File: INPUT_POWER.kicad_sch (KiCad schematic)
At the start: 26 parts, among them J1 TYPE-C-31-M12_13, SW3 ON/OFF, U3 IP5306

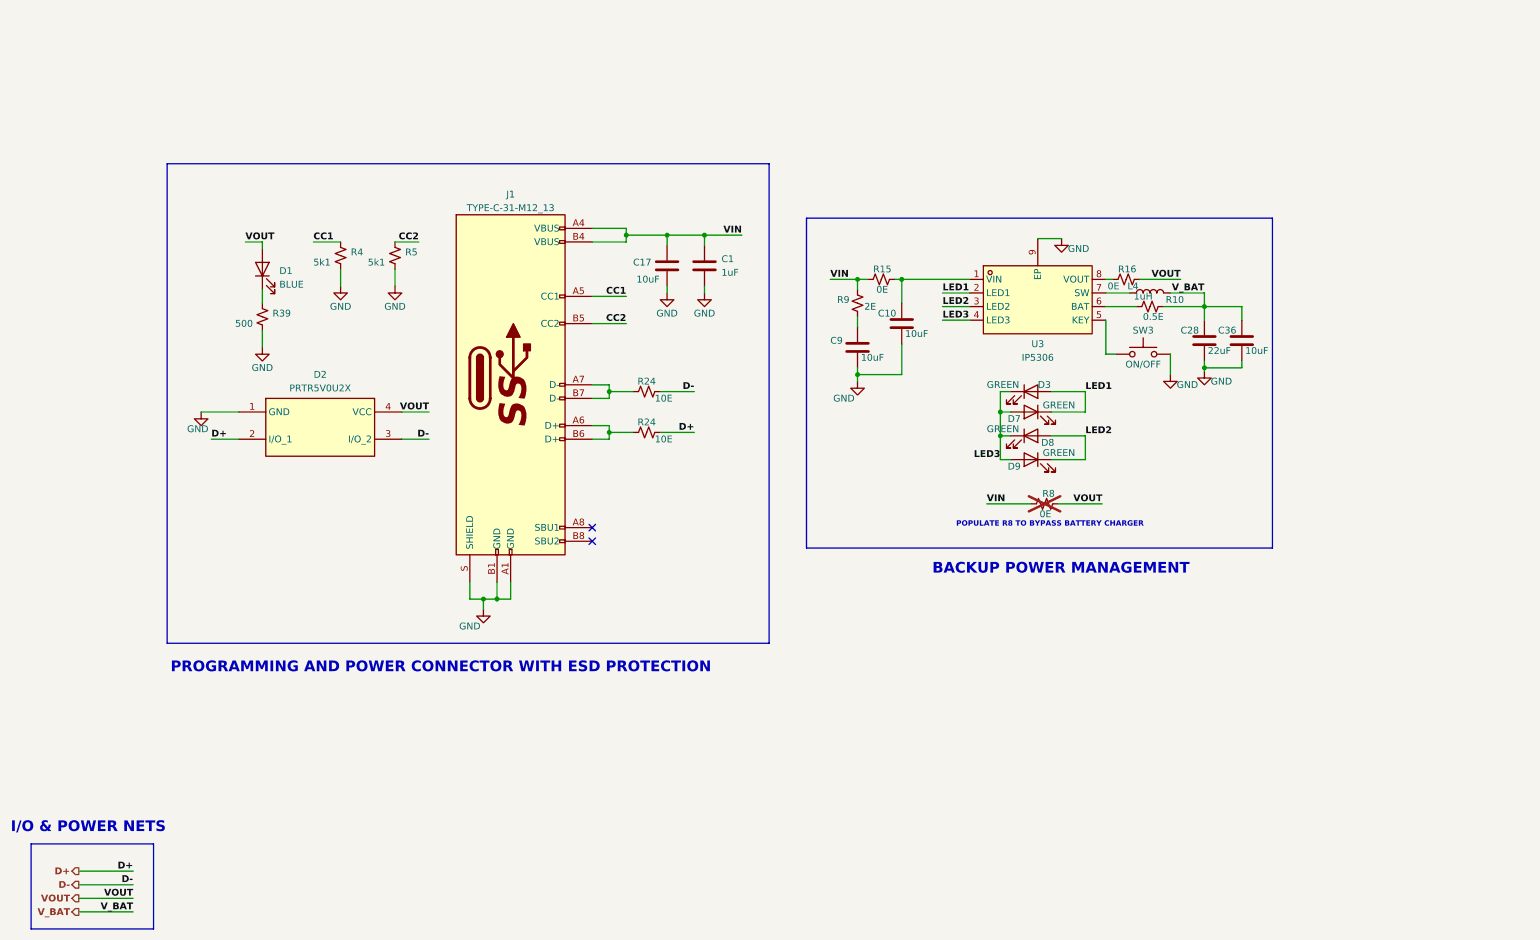
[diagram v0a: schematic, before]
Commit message: Corrected schematic to PCB export error and warings and IP5306 and SD card section
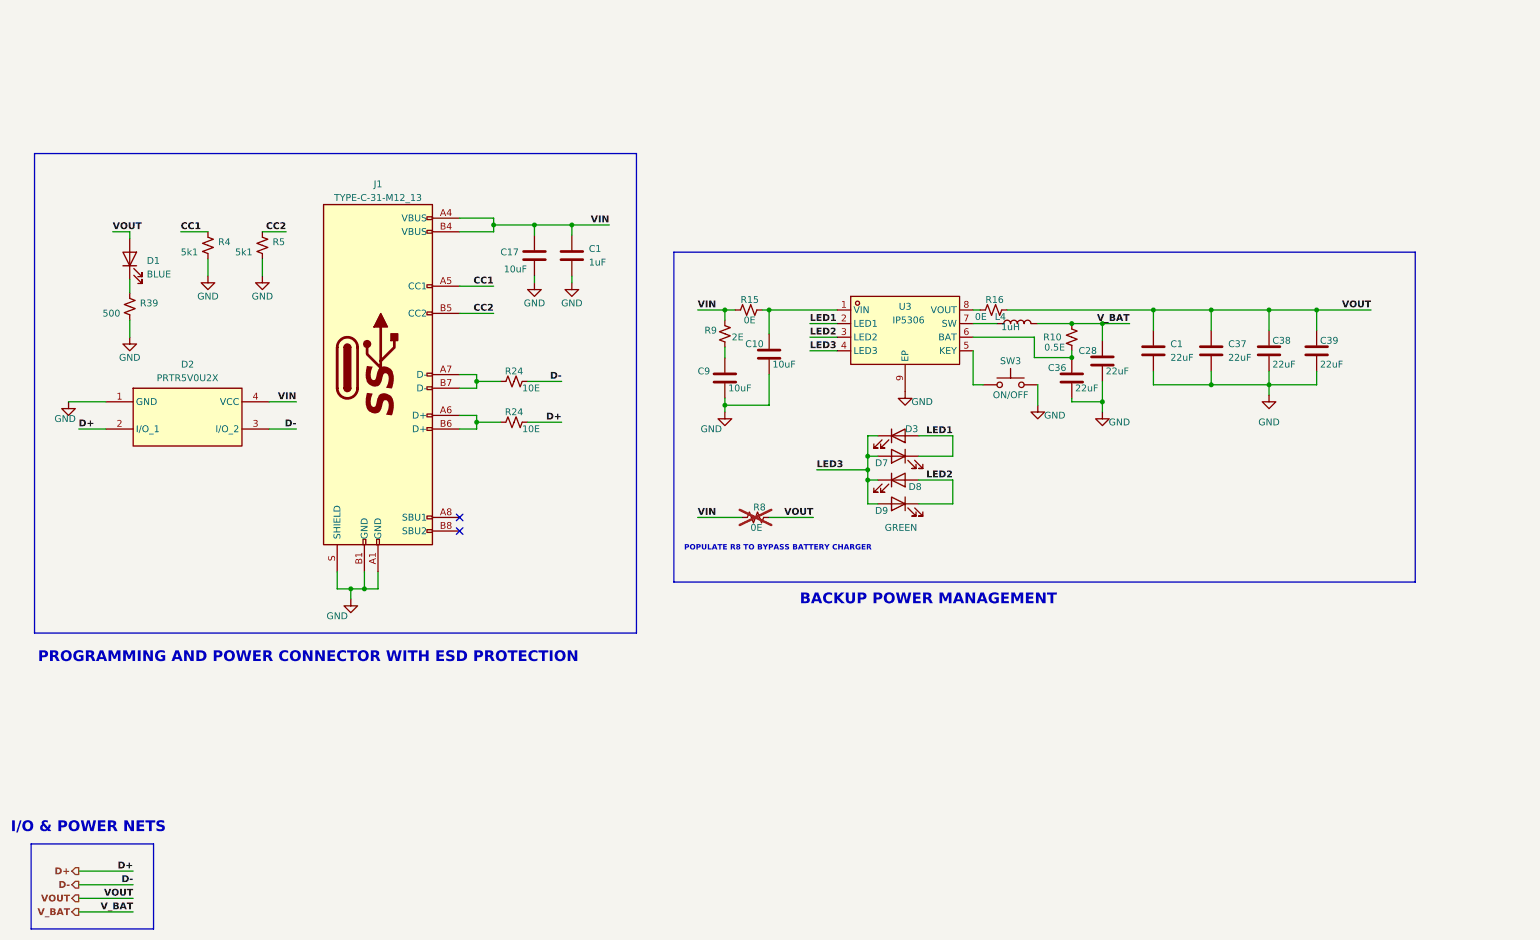
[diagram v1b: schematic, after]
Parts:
- added C1, C37, C38, C39: 22uF, ESP32-S3_Dev_Board:C_1206_3216Metric, symbol ESP32-S3_DB:C
- C36: value 10uF -> 22uF; footprint ESP32-S3_Dev_Board:C_0805_2012Metric -> ESP32-S3_Dev_Board:C_0603_1608Metric; PN CL21A106KAYNNNE -> CL10A226MO7JZNC
- U3: footprint ESP32-S3_Dev_Board:ESOP-8_L4.9-W3.9-P1.27-LS6.0-BL-EP -> ESP32-S3_Dev_Board:ESOP-8
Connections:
- net GND: now also C1.2, C37.2, C38.2, C39.2
- net VIN: now also D2.4 (VCC)
- net VOUT: now also C1.1, C37.1, C38.1, C39.1; no longer D2.4 (VCC)
- net V_BAT: no longer C36.1
- net at R10.1, U3.6 (BAT): now also C36.1
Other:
- moved on the sheet: C1, C10, C17, C28, C9, D1, D2, D3, D7, D8, D9, J1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

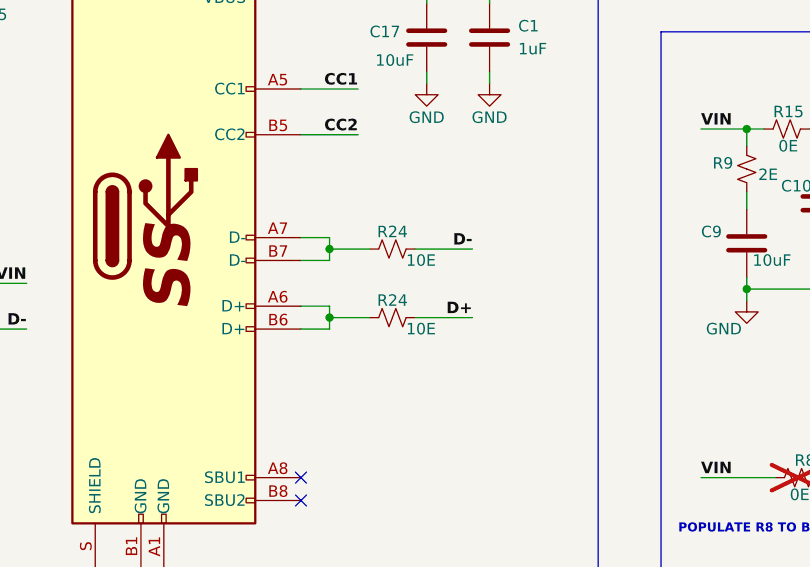
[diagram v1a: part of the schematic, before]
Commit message: Changes CH340 schematic
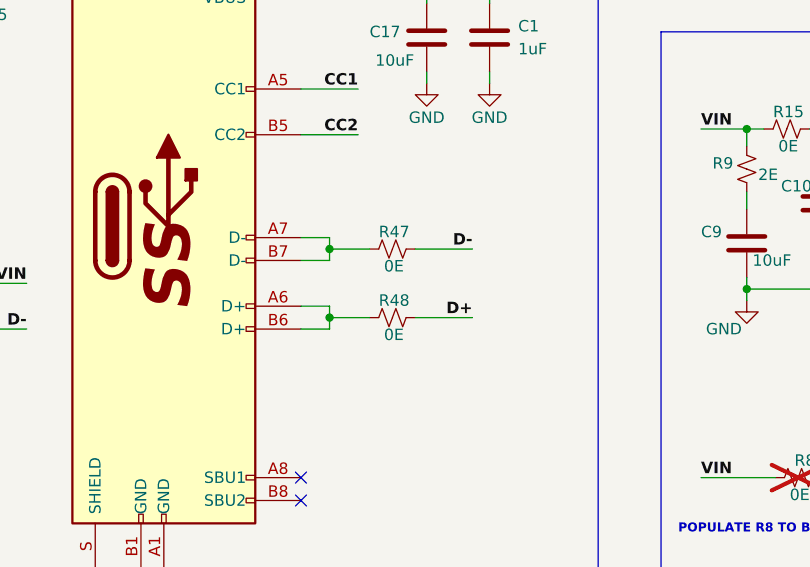
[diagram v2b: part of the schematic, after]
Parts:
- removed R24 (x2): 10E, ESP32-S3_Dev_Board:R_0402_1005Metric, symbol ESP32-S3_DB:R_Small_US
- added R47, R48: 0E, ESP32-S3_Dev_Board:R_0603_1608Metric, symbol ESP32-S3_DB:R_Small_US
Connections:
- net D+: now also R48.2
- net D-: now also R47.2
- net at J1.A7 (D-), J1.B7 (D-): now also R47.1
- net at J1.A6 (D+), J1.B6 (D+): now also R48.1
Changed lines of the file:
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@@
-    )
-  )
-  (symbol (lib_id "ESP32-S3_DB:R_Small_US") (at 109.855 86.36 90) (unit 1)
-    (in_bom yes) (on_board yes) (dnp no)
-    (property "Reference" "R24" (at 109.855 84.455 90)
-      (effects (font (size 1.27 1.27)))
-    )
-    (property "Value" "10E" (at 113.03 87.63 90)
-      (effects (font (size 1.27 1.27)))
-    )
-    (property "Footprint" "ESP32-S3_Dev_Board:R_0402_1005Metric" (at 109.855 86.36 0)
-      (effects (font (size 1.27 1.27)) hide)
-    )
-    (property "Datasheet" "~" (at 109.855 86.36 0)
-      (effects (font (size 1.27 1.27)) hide)
-    )
-    (property "PN" "RTT02100JTH" (at 109.855 86.36 0)
-      (effects (font (size 1.27 1.27)) hide)
-    )
-    (pin "1")
-    (pin "2")
-    (instances
-      (project "ESP32-S3_DB"
-        (path "/b7fc4bd3-c219-4455-832b-8d795385dcf1/9b4afe2f-79e5-4a56-98d7-d16b193c0e70"
-          (reference "R24") (unit 1)
-        )
-        (path "/b7fc4bd3-c219-4455-832b-8d795385dcf1/95090a63-7b3c-4ea0-92b8-aeafe05264cd"
-          (reference "R47") (unit 1)
-        )
-      )
-    )
-  )
-  (symbol (lib_id "ESP32-S3_DB:R_Small_US") (at 109.855 93.98 90) (unit 1)
-    (in_bom yes) (on_board yes) (dnp no)
-    (property "Reference" "R24" (at 109.855 92.075 90)
-      (effects (font (size 1.27 1.27)))
-    )
-    (property "Value" "10E" (at 113.03 95.25 90)
-      (effects (font (size 1.27 1.27)))
-    )
-    (property "Footprint" "ESP32-S3_Dev_Board:R_0402_1005Metric" (at 109.855 93.98 0)
-      (effects (font (size 1.27 1.27)) hide)
-    )
-    (property "Datasheet" "~" (at 109.855 93.98 0)
-      (effects (font (size 1.27 1.27)) hide)
-    )
-    (property "PN" "RTT02100JTH" (at 109.855 93.98 0)
-      (effects (font (size 1.27 1.27)) hide)
-    )
-    (pin "1")
-    (pin "2")
-    (instances
-      (project "ESP32-S3_DB"
-        (path "/b7fc4bd3-c219-4455-832b-8d795385dcf1/9b4afe2f-79e5-4a56-98d7-d16b193c0e70"
-          (reference "R24") (unit 1)
-        )
-        (path "/b7fc4bd3-c219-4455-832b-8d795385dcf1/95090a63-7b3c-4ea0-92b8-aeafe05264cd"
-          (reference "R48") (unit 1)
-        )
-      )
     )
   )
@@
         (path "/b7fc4bd3-c219-4455-832b-8d795385dcf1/95090a63-7b3c-4ea0-92b8-aeafe05264cd"
           (reference "R5") (unit 1)
+        )
+      )
+    )
+  )
+  (symbol (lib_id "ESP32-S3_DB:R_Small_US") (at 109.855 93.98 90) (unit 1)
+    (in_bom yes) (on_board yes) (dnp no)
+    (property "Reference" "R48" (at 111.76 92.075 90)
+      (effects (font (size 1.27 1.27)) (justify left))
+    )
+    (property "Value" "0E" (at 111.125 95.885 90)
+      (effects (font (size 1.27 1.27)) (justify left))
+    )
+    (property "Footprint" "ESP32-S3_Dev_Board:R_0603_1608Metric" (at 109.855 93.98 0)
+      (effects (font (size 1.27 1.27)) hide)
+    )
+    (property "Datasheet" "~" (at 109.855 93.98 0)
+      (effects (font (size 1.27 1.27)) hide)
+    )
+    (property "PN" "RC0603JR-070RL" (at 109.855 93.98 0)
+      (effects (font (size 1.27 1.27)) hide)
+    )
+    (pin "1")
+    (pin "2")
+    (instances
+      (project "ESP32-S3_DB"
+        (path "/b7fc4bd3-c219-4455-832b-8d795385dcf1/95090a63-7b3c-4ea0-92b8-aeafe05264cd"
+          (reference "R48") (unit 1)
         )
       )
@@
         )
       )
+    )
+  )
+  (symbol (lib_id "ESP32-S3_DB:R_Small_US") (at 109.855 86.36 90) (unit 1)
+    (in_bom yes) (on_board yes) (dnp no)
+    (property "Reference" "R47" (at 111.76 84.455 90)
+      (effects (font (size 1.27 1.27)) (justify left))
+    )
+    (property "Value" "0E" (at 111.125 88.265 90)
+      (effects (font (size 1.27 1.27)) (justify left))
+    )
+    (property "Footprint" "ESP32-S3_Dev_Board:R_0603_1608Metric" (at 109.855 86.36 0)
+      (effects (font (size 1.27 1.27)) hide)
+    )
+    (property "Datasheet" "~" (at 109.855 86.36 0)
+      (effects (font (size 1.27 1.27)) hide)
+    )
+    (property "PN" "RC0603JR-070RL" (at 109.855 86.36 0)
+      (effects (font (size 1.27 1.27)) hide)
+    )
+    (pin "1")
+    (pin "2")
+    (instances
+      (project "ESP32-S3_DB"
+        (path "/b7fc4bd3-c219-4455-832b-8d795385dcf1/95090a63-7b3c-4ea0-92b8-aeafe05264cd"
+          (reference "R47") (unit 1)
+        )
+      )

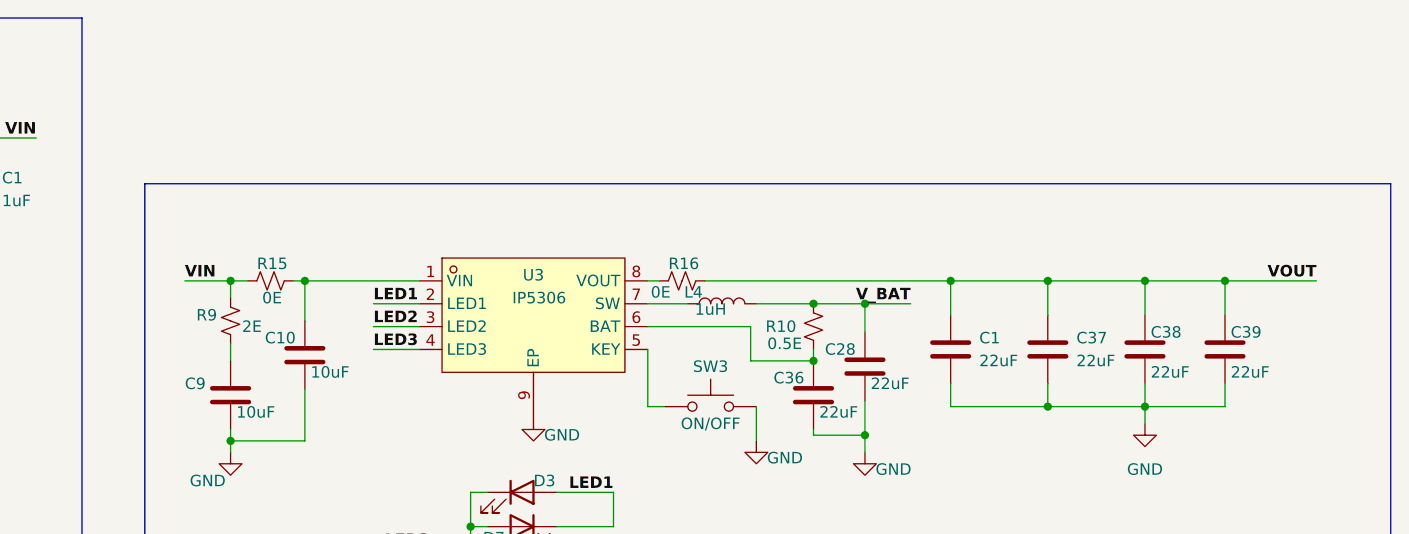
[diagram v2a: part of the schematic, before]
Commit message: Arranged IP5306, Added support for USB-To-RS485
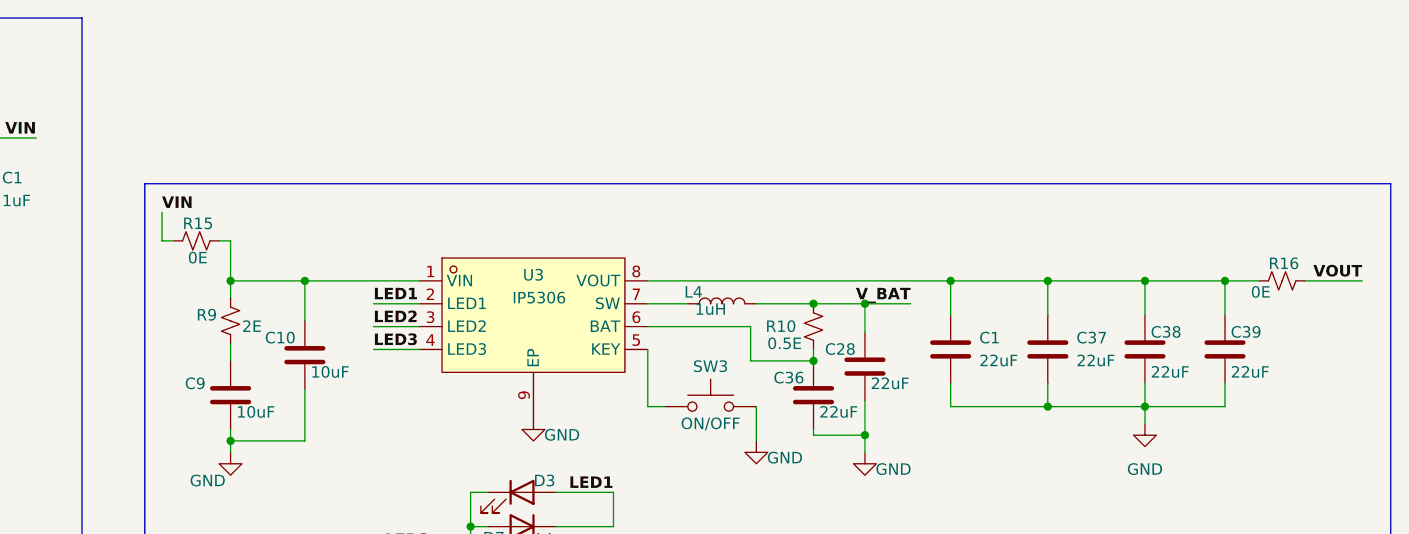
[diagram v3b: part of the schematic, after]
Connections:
- net VIN: no longer R9.1
- net VOUT: no longer C1.1, C37.1, C38.1, C39.1
- net at R16.1, U3.8 (VOUT): now also C1.1, C37.1, C38.1, C39.1
- net at C10.1, R15.2, U3.1 (VIN): now also R9.1
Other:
- moved on the sheet: R15, R16
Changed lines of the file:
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@@
     (stroke (width 1) (type default) (color 72 72 72 1))
   )
-  (wire (pts (xy 201.93 73.025) (xy 229.235 73.025))
+  (wire (pts (xy 195.58 73.025) (xy 229.235 73.025))
     (stroke (width 0) (type default))
   )
@@
     (stroke (width 0) (type default))
   )
+  (wire (pts (xy 141.605 65.405) (xy 141.605 68.58))
+    (stroke (width 0) (type default))
+  )
   (wire (pts (xy 149.225 74.93) (xy 149.225 73.025))
     (stroke (width 0) (type default))
@@
     (stroke (width 0.5) (type default) (color 0 0 255 1))
   )
-  (wire (pts (xy 196.85 73.025) (xy 195.58 73.025))
-    (stroke (width 0) (type default))
-  )
   (wire (pts (xy 165.1 75.565) (xy 170.18 75.565))
     (stroke (width 0) (type default))
@@
     (stroke (width 0.5) (type default) (color 255 0 0 1))
   )
+  (wire (pts (xy 141.605 68.58) (xy 142.875 68.58))
+    (stroke (width 0) (type default))
+  )
   (wire (pts (xy 207.645 90.805) (xy 207.645 86.995))
     (stroke (width 0) (type default))
@@
   )
   (wire (pts (xy 144.145 111.76) (xy 152.4 111.76))
+    (stroke (width 0) (type default))
+  )
+  (wire (pts (xy 147.955 68.58) (xy 149.225 68.58))
     (stroke (width 0) (type default))
   )
@@
     (stroke (width 0) (type default))
   )
-  (wire (pts (xy 156.21 73.025) (xy 157.48 73.025))
-    (stroke (width 0) (type default))
-  )
   (wire (pts (xy 67.31 58.42) (xy 62.865 58.42))
     (stroke (width 0) (type default))
   )
   (wire (pts (xy 102.87 86.36) (xy 102.87 87.63))
+    (stroke (width 0) (type default))
+  )
+  (wire (pts (xy 268.605 73.025) (xy 274.955 73.025))
     (stroke (width 0) (type default))
   )
@@
     (stroke (width 0) (type default))
   )
-  (wire (pts (xy 144.145 73.025) (xy 149.225 73.025))
-    (stroke (width 0) (type default))
-  )
   (wire (pts (xy 106.045 58.42) (xy 99.695 58.42))
     (stroke (width 0) (type default))
@@
     (stroke (width 0) (type default))
   )
-  (wire (pts (xy 259.715 73.025) (xy 269.875 73.025))
-    (stroke (width 0) (type default))
-  )
-  (wire (pts (xy 149.225 73.025) (xy 151.13 73.025))
+  (wire (pts (xy 259.715 73.025) (xy 263.525 73.025))
+    (stroke (width 0) (type default))
+  )
+  (wire (pts (xy 149.225 73.025) (xy 157.48 73.025))
+    (stroke (width 0) (type default))
+  )
+  (wire (pts (xy 149.225 68.58) (xy 149.225 73.025))
     (stroke (width 0) (type default))
   )
@@
     (effects (font (size 1.27 1.27) (thickness 0.254) bold (color 0 0 255 1)) (justify left bottom))
   )
-  (label "VOUT" (at 269.875 73.025 180) (fields_autoplaced)
+  (label "VOUT" (at 274.955 73.025 180) (fields_autoplaced)
     (effects (font (size 1.27 1.27) bold (color 255 0 0 1)) (justify right bottom))
   )
-  (label "VIN" (at 144.145 73.025 0) (fields_autoplaced)
+  (label "VIN" (at 141.605 65.405 0) (fields_autoplaced)
     (effects (font (size 1.27 1.27) (thickness 0.254) bold (color 255 0 0 1)) (justify left bottom))
   )
@@
     )
   )
-  (symbol (lib_id "ESP32-S3_DB:R_Small_US") (at 199.39 73.025 90) (unit 1)
-    (in_bom yes) (on_board yes) (dnp no)
-    (property "Reference" "R16" (at 201.295 71.12 90)
-      (effects (font (size 1.27 1.27)) (justify left))
-    )
-    (property "Value" "0E" (at 198.12 74.295 90)
-      (effects (font (size 1.27 1.27)) (justify left))
-    )
-    (property "Footprint" "ESP32-S3_Dev_Board:R_0603_1608Metric" (at 199.39 73.025 0)
-      (effects (font (size 1.27 1.27)) hide)
-    )
-    (property "Datasheet" "~" (at 199.39 73.025 0)
-      (effects (font (size 1.27 1.27)) hide)
-    )
-    (property "PN" "RC0603JR-070RL" (at 199.39 73.025 0)
+  (symbol (lib_id "ESP32-S3_DB:R_Small_US") (at 266.065 73.025 90) (unit 1)
+    (in_bom yes) (on_board yes) (dnp no)
+    (property "Reference" "R16" (at 267.97 71.12 90)
+      (effects (font (size 1.27 1.27)) (justify left))
+    )
+    (property "Value" "0E" (at 264.795 74.295 90)
+      (effects (font (size 1.27 1.27)) (justify left))
+    )
+    (property "Footprint" "ESP32-S3_Dev_Board:R_0603_1608Metric" (at 266.065 73.025 0)
+      (effects (font (size 1.27 1.27)) hide)
+    )
+    (property "Datasheet" "~" (at 266.065 73.025 0)
+      (effects (font (size 1.27 1.27)) hide)
+    )
+    (property "PN" "RC0603JR-070RL" (at 266.065 73.025 0)
       (effects (font (size 1.27 1.27)) hide)
     )
@@
     )
   )
-  (symbol (lib_id "ESP32-S3_DB:R_Small_US") (at 153.67 73.025 90) (unit 1)
-    (in_bom yes) (on_board yes) (dnp no)
-    (property "Reference" "R15" (at 155.575 71.12 90)
-      (effects (font (size 1.27 1.27)) (justify left))
-    )
-    (property "Value" "0E" (at 154.94 74.93 90)
-      (effects (font (size 1.27 1.27)) (justify left))
-    )
-    (property "Footprint" "ESP32-S3_Dev_Board:R_0603_1608Metric" (at 153.67 73.025 0)
-      (effects (font (size 1.27 1.27)) hide)
-    )
-    (property "Datasheet" "~" (at 153.67 73.025 0)
-      (effects (font (size 1.27 1.27)) hide)
-    )
-    (property "PN" "RC0603JR-070RL" (at 153.67 73.025 0)
-      (effects (font (size 1.27 1.27)) hide)
-    )
+  (symbol (lib_id "ESP32-S3_DB:R_Small_US") (at 145.415 68.58 90) (unit 1)
+    (in_bom yes) (on_board yes) (dnp no)
+    (property "Reference" "R15" (at 147.32 66.675 90)
+      (effects (font (size 1.27 1.27)) (justify left))
+    )
+    (property "Value" "0E" (at 146.685 70.485 90)
+      (effects (font (size 1.27 1.27)) (justify left))
+    )
+    (property "Footprint" "ESP32-S3_Dev_Board:R_0603_1608Metric" (at 145.415 68.58 0)
+      (effects (font (size 1.27 1.27)) hide)
+    )
+    (property "Datasheet" "~" (at 145.415 68.58 0)
+      (effects (font (size 1.27 1.27)) hide)
+    )
+    (property "PN" "RC0603JR-070RL" (at 145.415 68.58 0)
+      (effects (font (size 1.27 1.27)) hide)
+    )
